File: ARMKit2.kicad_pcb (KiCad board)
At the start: 2 copper layers, 36 parts, among them P1 CONN_01X06, P2 CONN_01X32, P3 CONN_01X32, P4 USB_B, U1 STM32F405RG, U2 LT1761, Y1 Crystal, Y2 Crystal

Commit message: Added a bunch of traces
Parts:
- moved R1 50.0 mm to (89.8, 95.5)
- moved C20 34.7 mm to (55.2, 133.0), turned to 90 degrees
- moved C19 30.5 mm to (58.8, 133.5), turned to 90 degrees
- moved U2 26.5 mm to (62.1, 133.3), turned to 180 degrees
- moved C18 21.9 mm to (66.7, 134.0), turned to 270 degrees
- moved P1 17.5 mm to (85.0, 134.6), turned to 90 degrees
- moved D2 13.3 mm to (68.8, 127.9), turned to 0 degrees
- moved C16 2.06 mm to (81.6, 113.7), turned to 270 degrees
- moved P4 2.04 mm to (75.4, 134.7)
- moved C17 1.74 mm to (83.9, 113.7), turned to 270 degrees
- moved D1 1.48 mm to (73.2, 118.7)
- moved R4 1.48 mm to (73.2, 123.1), turned to 270 degrees
- moved D4 1.17 mm to (75.9, 118.7)
- moved R5 1.17 mm to (75.9, 123.1)
- moved C14 0.85 mm to (84.1, 96.9)
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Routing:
- net PA8: track 0.00 -> 29.2 mm
- net PC9: track 0.00 -> 28.8 mm
- net PA10: track 0.00 -> 27.3 mm
- net PC7: track 0.00 -> 27.0 mm
- net PC8: track 0.00 -> 26.5 mm
- net PA12: track 0.00 -> 26.2 mm
- net PA9: track 0.00 -> 25.2 mm
- net PB15: track 0.00 -> 24.6 mm
- net NRST: track 3.67 -> 27.8 mm
- net PA11: track 0.00 -> 23.9 mm
- net PC13: track 0.00 -> 22.8 mm
- net PC6: track 0.00 -> 22.7 mm
- net PB13: track 0.00 -> 22.3 mm
- net PB14: track 0.00 -> 20.4 mm
- net PB11: track 0.00 -> 19.9 mm
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
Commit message: More layout work.
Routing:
- net VDD1: track 28.5 -> 256.7 mm, vias 0 -> 9
- net NRST: track 27.8 -> 75.5 mm
- net SWCLK: track 19.1 -> 56.9 mm
- net TRACESWO: track 17.5 -> 50.9 mm
- net SWDIO: track 19.8 -> 49.6 mm
- net PB14: track 20.4 -> 37.6 mm, vias 0 -> 2
- net PB15: track 24.6 -> 41.6 mm, vias 0 -> 2
- net GND: track 33.2 -> 48.8 mm, vias 8 -> 16
- net 5V_IN: track 0.00 -> 11.4 mm
- net Net-(D2-Pad2): track 0.00 -> 5.54 mm
- net Net-(C19-Pad2): track 0.00 -> 2.23 mm
- added copper zone on F.Cu, net VDD1

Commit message: Finalized PCB
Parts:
- added REF**: MountingHole_3mm, Mounting_Holes:MountingHole_3mm, F.Cu at (50.8, 83.8)
- added REF**: MountingHole_3mm, Mounting_Holes:MountingHole_3mm, F.Cu at (101.6, 83.8)
- added REF**: MountingHole_3mm, Mounting_Holes:MountingHole_3mm, F.Cu at (101.6, 137.2)
- added REF**: MountingHole_3mm, Mounting_Holes:MountingHole_3mm, F.Cu at (50.8, 137.2)
- moved R1 1.40 mm to (88.4, 95.4)
- moved C8 0.51 mm to (90.7, 85.9)
- moved Y2 0.51 mm to (89.1, 89.8)
- moved C9 0.51 mm to (87.4, 85.9)
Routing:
- net NRST: track 75.5 -> 77.1 mm
- net VDD1: track 256.7 -> 255.3 mm
- net GND: track 48.8 -> 49.9 mm, vias 16 -> 17
- net OSC32_IN: track 21.6 -> 21.1 mm
- net OSC32_OUT: track 18.4 -> 17.9 mm
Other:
- board text added: "BOOT0"
- board text added: "CLK"
- board text added: "GND"
- board text added: "NRST"
- board text added: "PA0"
- board text added: "PA1"
- board text added: "PA10"
- board text added: "PA11"
- board text added: "PA12"
- board text added: "PA15"
- board text added: "PA2"
- board text added: "PA3"
- board text added: "PA4"
- board text added: "PA5"
- board text added: "PA6"
- board text added: "PA7"
- board text added: "PA8"
- board text added: "PA9"
- board text added: "PB0"
- board text added: "PB1"
- board text added: "PB10"
- board text added: "PB11"
- board text added: "PB12"
- board text added: "PB13"
- board text added: "PB14"
- board text added: "PB15"
- board text added: "PB2"
- board text added: "PB4"
- board text added: "PB5"
- board text added: "PB6"
- board text added: "PB7"
- board text added: "PB8"
- board text added: "PB9"
- board text added: "PC0"
- board text added: "PC1"
- board text added: "PC10"
- board text added: "PC11"
- board text added: "PC12"
- board text added: "PC13"
- board text added: "PC2"
- board text added: "PC3"
- board text added: "PC4"
- board text added: "PC5"
- board text added: "PC6"
- board text added: "PC7"
- board text added: "PC8"
- board text added: "PC9"
- board text added: "PD2"
- board text added: "STM32 Breakout"
- board text added: "SWDIO"
- board text added: "SWO"
- board text added: "VDD"

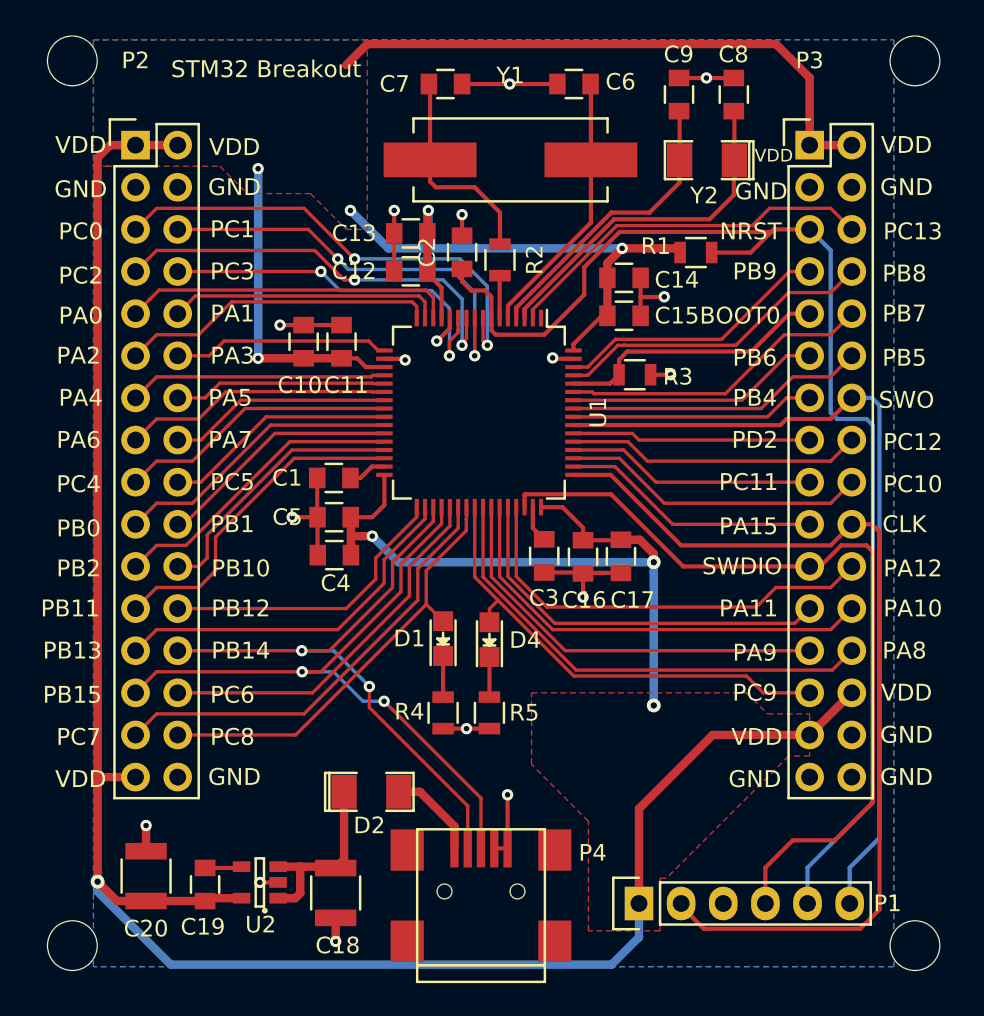
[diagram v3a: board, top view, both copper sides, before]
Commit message: Added some detail on the silk layer
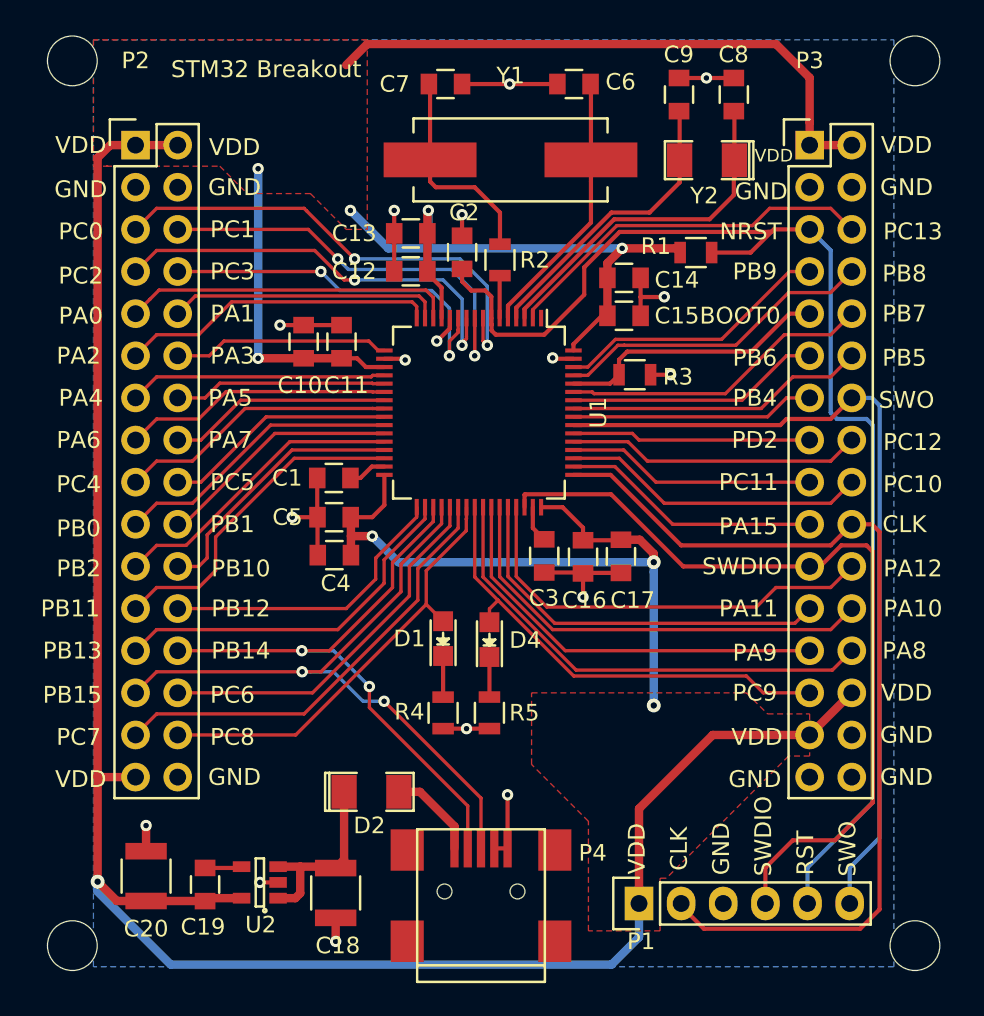
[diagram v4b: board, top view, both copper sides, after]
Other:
- board text added: "RST"
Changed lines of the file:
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@@
     (area 44.359074 80.477099 110.042446 143.08866)
     (thickness 1.6)
-    (drawings 69)
+    (drawings 75)
     (tracks 519)
     (zones 0)
@@
     (tags "capacitor 0805")
     (attr smd)
-    (fp_text reference C2 (at 0 -2.1 90) (layer F.SilkS)
+    (fp_text reference C2 (at 2.397 0.127 180) (layer F.SilkS)
       (effects (font (size 1 1) (thickness 0.15)))
     )
@@
     (descr "Through hole pin header")
     (tags "pin header")
-    (fp_text reference P1 (at 0 14.986 180) (layer F.SilkS)
+    (fp_text reference P1 (at -2.286 0.127 180) (layer F.SilkS)
       (effects (font (size 1 1) (thickness 0.15)))
     )
@@
     (tags "resistor 0805")
     (attr smd)
-    (fp_text reference R2 (at 0 -2.1 270) (layer F.SilkS)
+    (fp_text reference R2 (at 0 -2.1 360) (layer F.SilkS)
       (effects (font (size 1 1) (thickness 0.15)))
     )
@@
     (pad 1 thru_hole circle (at 0 0) (size 3 3) (drill 3) (layers))
   )
+  (gr_text SWO (at 97.536 131.318 90) (layer F.SilkS)
+    (effects (font (size 1.016 1.016) (thickness 0.2032)))
+  )
+  (gr_text RST (at 94.996 131.572 90) (layer F.SilkS)
+    (effects (font (size 1.016 1.016) (thickness 0.2032)))
+  )
+  (gr_text SWDIO (at 92.456 130.556 90) (layer F.SilkS)
+    (effects (font (size 1.016 1.016) (thickness 0.2032)))
+  )
+  (gr_text GND (at 89.916 131.318 90) (layer F.SilkS)
+    (effects (font (size 1.016 1.016) (thickness 0.2032)))
+  )
+  (gr_text CLK (at 87.376 131.318 90) (layer F.SilkS)
+    (effects (font (size 1.016 1.016) (thickness 0.2032)))
+  )
+  (gr_text VDD (at 84.836 131.318 90) (layer F.SilkS)
+    (effects (font (size 1.016 1.016) (thickness 0.2032)))
+  )
   (gr_text "STM32 Breakout" (at 62.484 84.328) (layer F.SilkS)

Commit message: Added VBAT to breakout header, cleaned up RES fp size, cleaned up silkscreen
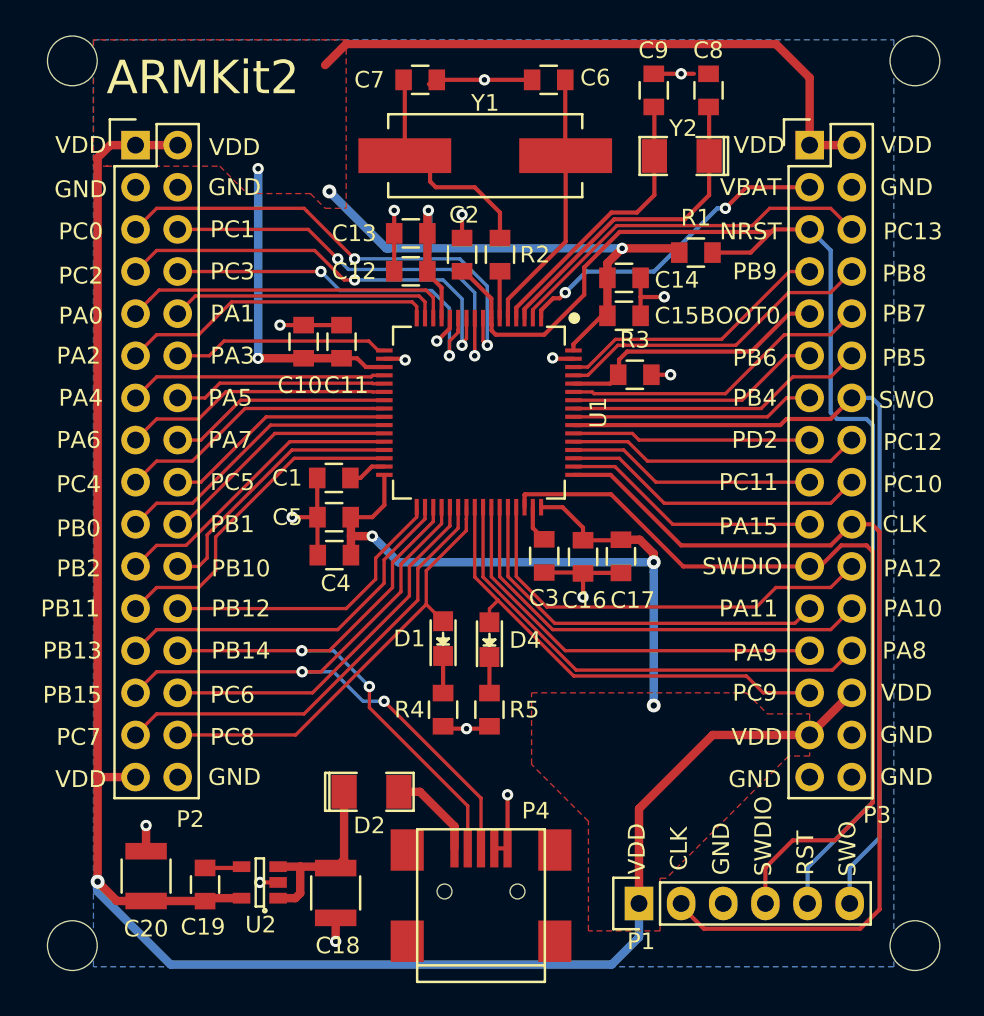
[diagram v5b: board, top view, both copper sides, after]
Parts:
- R1, R2, R3, R4, R5: footprint Resistors_SMD:R_0805 -> Capacitors_SMD:C_0805
- moved C6 1.55 mm to (79.5, 85.0)
- moved C7 1.55 mm to (71.8, 85.0)
- moved C8 1.55 mm to (89.2, 85.6)
- moved C9 1.55 mm to (85.9, 85.6)
- moved Y1 1.55 mm to (75.7, 89.5)
- moved Y2 1.55 mm to (87.5, 89.6)
- moved R2 0.31 mm to (76.6, 95.5)
- moved R4 0.19 mm to (73.2, 122.9)
- moved R5 0.19 mm to (75.9, 122.9)
- moved C2 0.14 mm to (74.3, 95.5)
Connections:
- P3 pad 3: GND -> VBAT
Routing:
- net VBAT: track 0.00 -> 19.7 mm, vias 0 -> 2
- net VDD1: track 255.3 -> 258.3 mm
- net OSC32_IN: track 21.1 -> 19.9 mm
- net GND: track 49.9 -> 49.1 mm
- net OSC32_OUT: track 17.9 -> 17.1 mm
- net NRST: track 77.1 -> 76.5 mm
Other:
- board text added: "ARMKit2"
- board text added: "VBAT"
- board text removed: "STM32 Breakout"

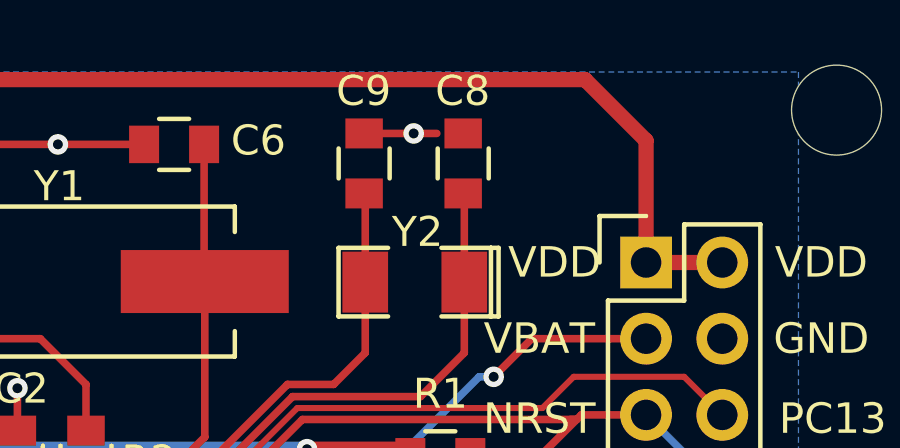
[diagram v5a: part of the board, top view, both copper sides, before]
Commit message: Fixed broken track
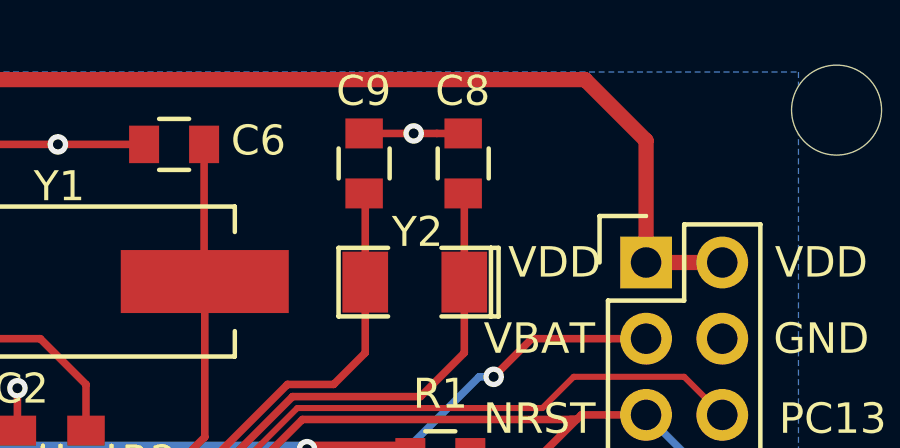
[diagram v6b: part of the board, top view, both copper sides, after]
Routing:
- net GND: track 49.1 -> 50.0 mm
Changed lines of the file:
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@@
   (general
     (links 140)
-    (no_connects 1)
-    (area 0 0 0 0)
+    (no_connects 0)
+    (area 44.359074 80.477099 110.042446 143.08866)
     (thickness 1.6)
     (drawings 75)
-    (tracks 528)
+    (tracks 529)
     (zones 0)
     (modules 40)
@@
   (gr_line (start 104.14 81.28) (end 104.14 139.7) (angle 90) (layer Dwgs.User) (width 0.2))
   (gr_line (start 48.26 81.28) (end 104.14 81.28) (angle 90) (layer Dwgs.User) (width 0.2))
+  (segment (start 88.275 84.598) (end 89.154 84.598) (width 0.254) (layer F.Cu) (net 1))
   (via (at 62.103 133.35) (size 0.6858) (drill 0.3302) (layers F.Cu B.Cu) (net 1))
   (segment (start 63.203 133.35) (end 62.103 133.35) (width 0.254) (layer F.Cu) (net 1))
